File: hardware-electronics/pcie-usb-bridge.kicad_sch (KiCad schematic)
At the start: 62 parts, among them U10 24AA04T-I_OT, U3 PI7C9X440SLBFDE, Y1 ABM8-12.000MHZ-B2-T

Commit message: SCH cosmetic changes
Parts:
- added TP16, TP17: ~, symbol M2SmartHomeSymbols:TP_SMD_1mm
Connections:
- net at U3.21 (SMBCLK): now also TP16.
- net at U3.64 (SMBDATA): now also TP17.
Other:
- moved on the sheet: FB9, TP1, TP2, TP3, TP8

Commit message: SCH fill info box
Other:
- title: (none) -> M2SmartHome
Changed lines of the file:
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@@
 	(generator_version "8.0")
 	(paper "A4")
+	(title_block
+		(title "M2SmartHome")
+		(date "2024-10-11")
+		(rev "Rev 1.0.0")
+	)
 	(junction
 		(at 173.99 85.09)

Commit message: SCH update all symbols
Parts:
- C1, C2: footprint M2SmartHomeFootprints:CAPC1005X56N -> M2SmartHomeFootprints:C_0402
- R1, R3, R50, R51, R52, R53, R54: footprint R_5k1_0402:R_0402_1005Metric -> M2SmartHomeFootprints:R_0402
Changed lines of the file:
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@@
 			)
 		)
-		(property "Footprint" "R_5k1_0402:R_0402_1005Metric"
+		(property "Footprint" "M2SmartHomeFootprints:R_0402"
 			(at 111.76 101.6 0)
 			(effects
@@
 			)
 		)
-		(property "Footprint" "R_5k1_0402:R_0402_1005Metric"
+		(property "Footprint" "M2SmartHomeFootprints:R_0402"
 			(at 99.06 124.46 0)
 			(effects
@@
 			)
 		)
-		(property "Footprint" "R_5k1_0402:R_0402_1005Metric"
+		(property "Footprint" "M2SmartHomeFootprints:R_0402"
 			(at 102.87 101.6 0)
 			(effects
@@
 			)
 		)
-		(property "Footprint" "R_5k1_0402:R_0402_1005Metric"
+		(property "Footprint" "M2SmartHomeFootprints:R_0402"
 			(at 93.98 101.6 0)
 			(effects
@@
 			)
 		)
-		(property "Footprint" "R_5k1_0402:R_0402_1005Metric"
+		(property "Footprint" "M2SmartHomeFootprints:R_0402"
 			(at 90.17 81.28 0)
 			(effects
@@
 			)
 		)
-		(property "Footprint" "M2SmartHomeFootprints:CAPC1005X56N"
+		(property "Footprint" "M2SmartHomeFootprints:C_0402"
 			(at 177.8 148.59 0)
 			(effects
@@
 			)
 		)
-		(property "Footprint" "R_5k1_0402:R_0402_1005Metric"
+		(property "Footprint" "M2SmartHomeFootprints:R_0402"
 			(at 101.6 81.28 0)
 			(effects
@@
 			)
 		)
-		(property "Footprint" "M2SmartHomeFootprints:CAPC1005X56N"
+		(property "Footprint" "M2SmartHomeFootprints:C_0402"
 			(at 213.36 148.59 0)
 			(effects
@@
 			)
 		)
-		(property "Footprint" "R_5k1_0402:R_0402_1005Metric"
+		(property "Footprint" "M2SmartHomeFootprints:R_0402"
 			(at 110.49 124.46 0)
 			(effects

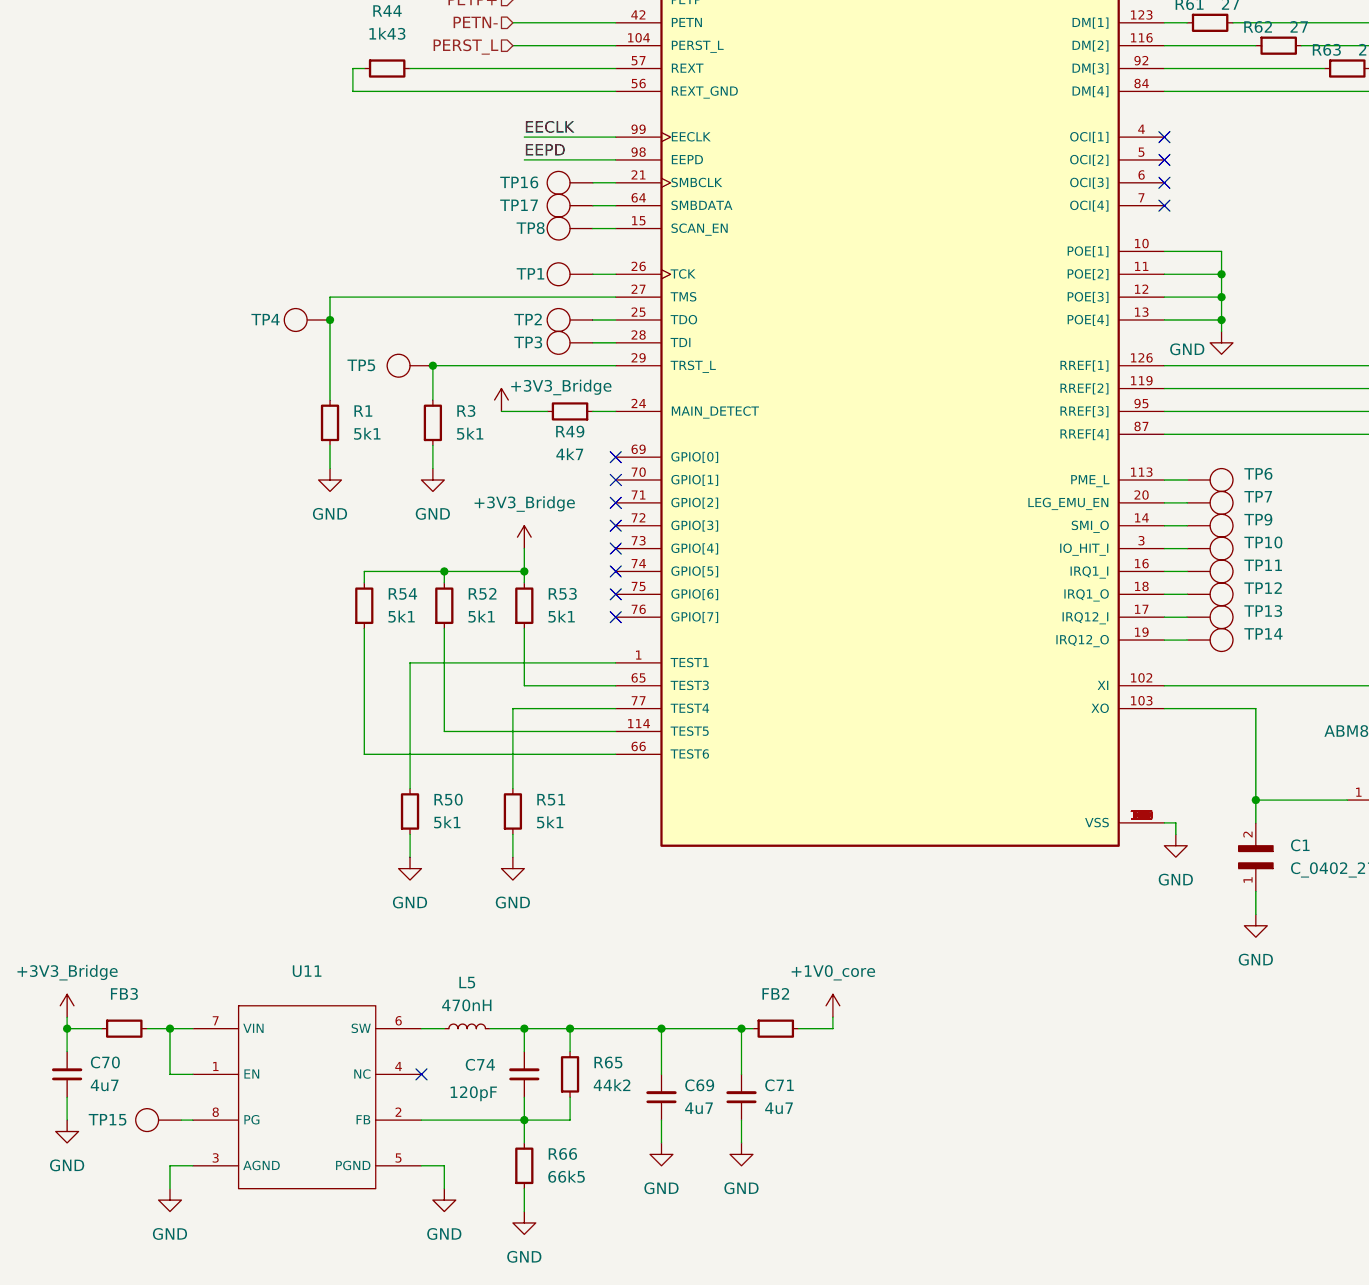
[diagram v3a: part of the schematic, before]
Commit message: [#13] BRD fix TP
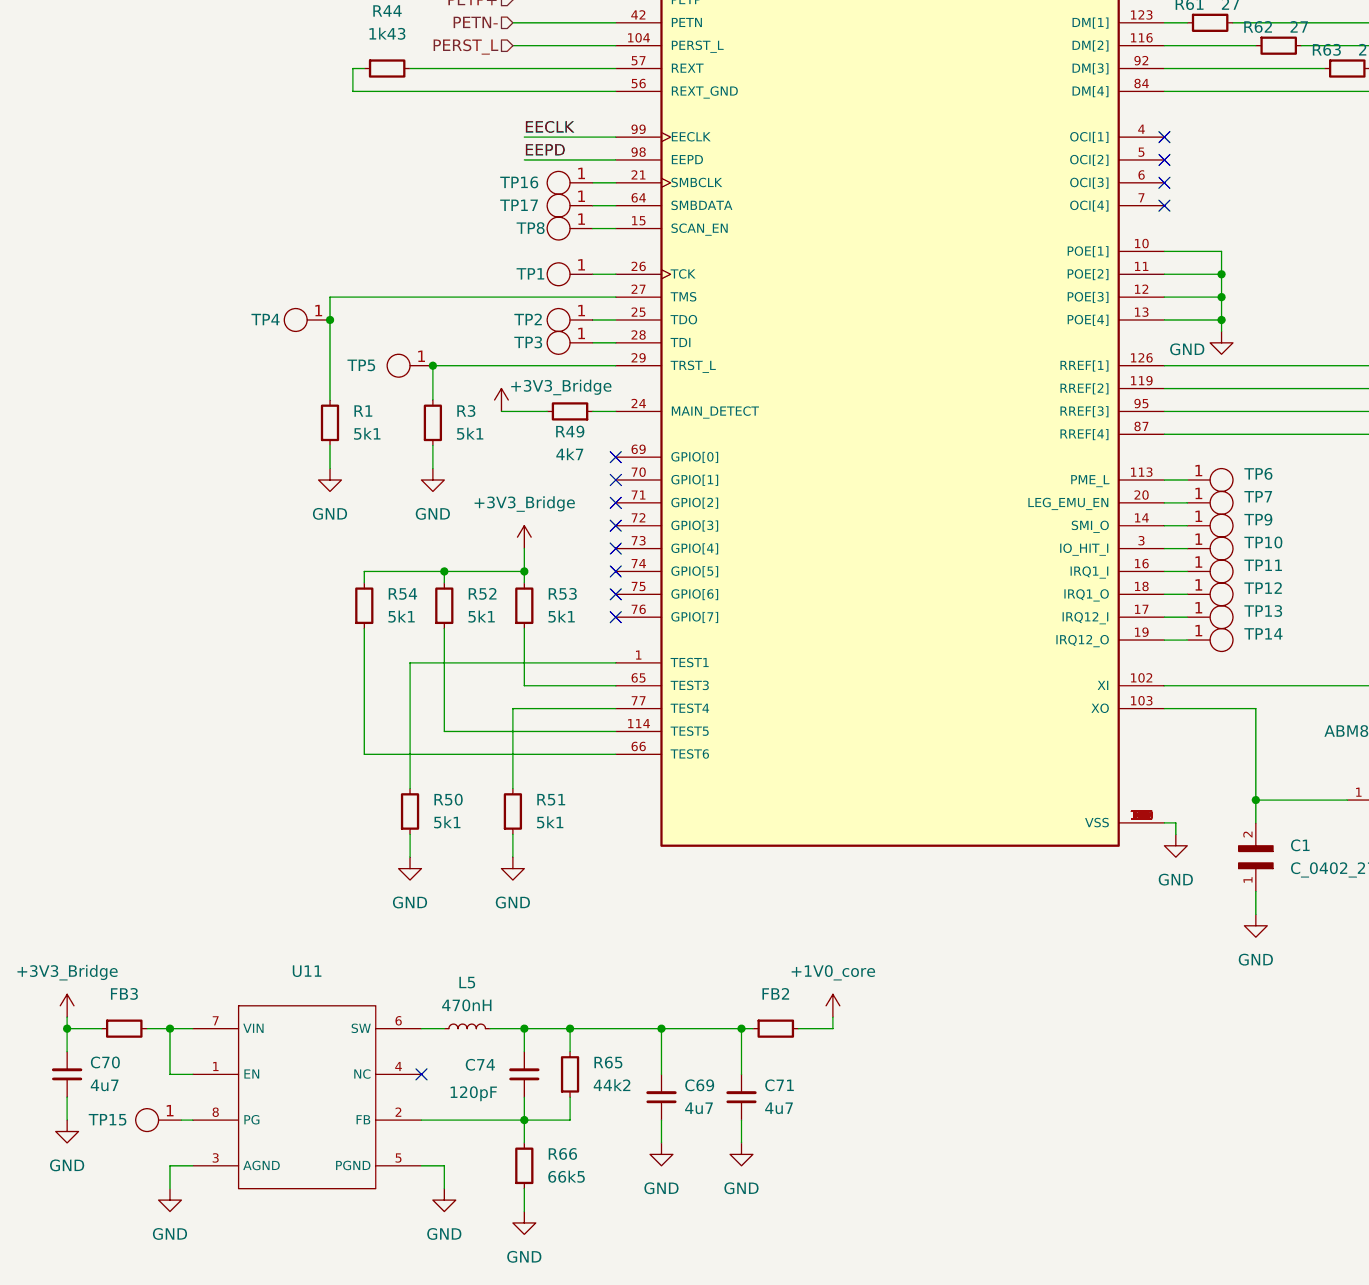
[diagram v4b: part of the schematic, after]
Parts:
- TP1, TP10, TP11, TP12, TP13, TP14, TP15, TP16, TP17, TP2, TP3, TP4, TP5, TP6, TP7, TP8, TP9: footprint (none) -> M2SmartHomeFootprints:TestPoint_Pad_D1.0mm
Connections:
- net at U3.21 (SMBCLK): now also TP16.1; no longer TP16.
- net at U11.8 (PG): now also TP15.1; no longer TP15.
- net at U3.20 (LEG_EMU_EN): now also TP7.1; no longer TP7.
- net at U3.25 (TDO): now also TP2.1; no longer TP2.
- net at U3.64 (SMBDATA): now also TP17.1; no longer TP17.
- net at U3.14 (SMI_O): now also TP9.1; no longer TP9.
- net at U3.15 (SCAN_EN): now also TP8.1; no longer TP8.
- net at U3.18 (IRQ1_O): now also TP12.1; no longer TP12.
- net at U3.17 (IRQ12_I): now also TP13.1; no longer TP13.
- net at U3.16 (IRQ1_I): now also TP11.1; no longer TP11.
- net at U3.3 (IO_HIT_I): now also TP10.1; no longer TP10.
- net at U3.19 (IRQ12_O): now also TP14.1; no longer TP14.
- net at R1.2, U3.27 (TMS): now also TP4.1; no longer TP4.
- net at U3.113 (PME_L): now also TP6.1; no longer TP6.
- net at R3.2, U3.29 (TRST_L): now also TP5.1; no longer TP5.
- net at U3.26 (TCK): now also TP1.1; no longer TP1.
- net at U3.28 (TDI): now also TP3.1; no longer TP3.
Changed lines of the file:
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@@
 			)
 		)
-		(property "Footprint" ""
+		(property "Footprint" "M2SmartHomeFootprints:TestPoint_Pad_D1.0mm"
 			(at 104.14 72.39 0)
 			(effects
@@
 			)
 		)
-		(pin ""
+		(pin "1"
 		)
 		(instances
@@
 			)
 		)
-		(property "Footprint" ""
+		(property "Footprint" "M2SmartHomeFootprints:TestPoint_Pad_D1.0mm"
 			(at 170.18 107.95 0)
 			(effects
@@
 			)
 		)
-		(pin ""
+		(pin "1"
 		)
 		(instances
@@
 			)
 		)
-		(property "Footprint" ""
+		(property "Footprint" "M2SmartHomeFootprints:TestPoint_Pad_D1.0mm"
 			(at 104.14 87.63 0)
 			(effects
@@
 			)
 		)
-		(pin ""
+		(pin "1"
 		)
 		(instances
@@
 			)
 		)
-		(property "Footprint" ""
+		(property "Footprint" "M2SmartHomeFootprints:TestPoint_Pad_D1.0mm"
 			(at 104.14 74.93 0)
 			(effects
@@
 			)
 		)
-		(pin ""
+		(pin "1"
 		)
 		(instances
@@
 			)
 		)
-		(property "Footprint" ""
+		(property "Footprint" "M2SmartHomeFootprints:TestPoint_Pad_D1.0mm"
 			(at 58.42 176.53 0)
 			(effects
@@
 			)
 		)
-		(pin ""
+		(pin "1"
 		)
 		(instances
@@
 			)
 		)
-		(property "Footprint" ""
+		(property "Footprint" "M2SmartHomeFootprints:TestPoint_Pad_D1.0mm"
 			(at 170.18 110.49 0)
 			(effects
@@
 			)
 		)
-		(pin ""
+		(pin "1"
 		)
 		(instances
@@
 			)
 		)
-		(property "Footprint" ""
+		(property "Footprint" "M2SmartHomeFootprints:TestPoint_Pad_D1.0mm"
 			(at 104.14 77.47 0)
 			(effects
@@
 			)
 		)
-		(pin ""
+		(pin "1"
 		)
 		(instances
@@
 			)
 		)
-		(property "Footprint" ""
+		(property "Footprint" "M2SmartHomeFootprints:TestPoint_Pad_D1.0mm"
 			(at 170.18 118.11 0)
 			(effects
@@
 			)
 		)
-		(pin ""
+		(pin "1"
 		)
 		(instances
@@
 			)
 		)
-		(property "Footprint" ""
+		(property "Footprint" "M2SmartHomeFootprints:TestPoint_Pad_D1.0mm"
 			(at 170.18 120.65 0)
 			(effects
@@
 			)
 		)
-		(pin ""
+		(pin "1"
 		)
 		(instances
@@
 			)
 		)
-		(property "Footprint" ""
+		(property "Footprint" "M2SmartHomeFootprints:TestPoint_Pad_D1.0mm"
 			(at 170.18 115.57 0)
 			(effects
@@
 			)
 		)
-		(pin ""
+		(pin "1"
 		)
 		(instances
@@
 			)
 		)
-		(property "Footprint" ""
+		(property "Footprint" "M2SmartHomeFootprints:TestPoint_Pad_D1.0mm"
 			(at 170.18 113.03 0)
 			(effects
@@
 			)
 		)
-		(pin ""
+		(pin "1"
 		)
 		(instances
@@
 			)
 		)
-		(property "Footprint" ""
+		(property "Footprint" "M2SmartHomeFootprints:TestPoint_Pad_D1.0mm"
 			(at 170.18 123.19 0)
 			(effects
@@
 			)
 		)
-		(pin ""
+		(pin "1"
 		)
 		(instances
@@
 			)
 		)
-		(property "Footprint" ""
+		(property "Footprint" "M2SmartHomeFootprints:TestPoint_Pad_D1.0mm"
 			(at 170.18 105.41 0)
 			(effects
@@
 			)
 		)
-		(pin ""
+		(pin "1"
 		)
 		(instances
@@
 			)
 		)
-		(property "Footprint" ""
+		(property "Footprint" "M2SmartHomeFootprints:TestPoint_Pad_D1.0mm"
 			(at 86.36 92.71 0)
 			(effects
@@
 			)
 		)
-		(pin ""
+		(pin "1"
 		)
 		(instances
@@
 			)
 		)
-		(property "Footprint" ""
+		(property "Footprint" "M2SmartHomeFootprints:TestPoint_Pad_D1.0mm"
 			(at 104.14 82.55 0)
 			(effects
@@
 			)
 		)
-		(pin ""
+		(pin "1"
 		)
 		(instances
@@
 			)
 		)
-		(property "Footprint" ""
+		(property "Footprint" "M2SmartHomeFootprints:TestPoint_Pad_D1.0mm"
 			(at 104.14 90.17 0)
 			(effects
@@
 			)
 		)
-		(pin ""
+		(pin "1"
 		)
 		(instances
@@
 			)
 		)
-		(property "Footprint" ""
+		(property "Footprint" "M2SmartHomeFootprints:TestPoint_Pad_D1.0mm"
 			(at 74.93 87.63 0)
 			(effects
@@
 			)
 		)
-		(pin ""
+		(pin "1"
 		)
 		(instances

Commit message: [#13] BRD fix 66k5 r and uSD slot
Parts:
- R66: footprint R_66k5_0402:R_0402_1005Metric -> M2SmartHomeFootprints:R_0402
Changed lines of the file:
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@@
 			)
 		)
-		(property "Footprint" "R_66k5_0402:R_0402_1005Metric"
+		(property "Footprint" "M2SmartHomeFootprints:R_0402"
 			(at 111.76 163.83 0)
 			(effects

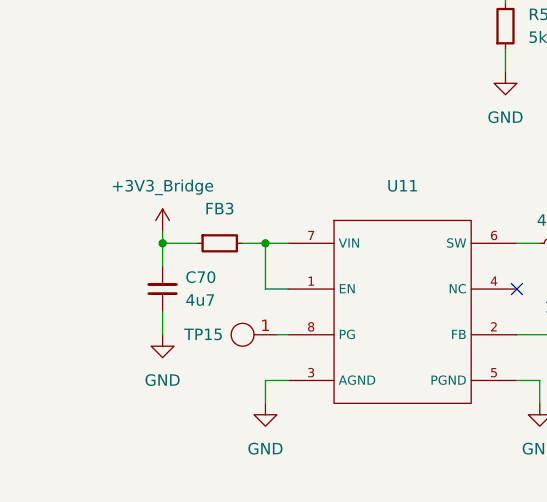
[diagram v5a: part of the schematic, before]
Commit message: [#13] WIP Placement PCIe bridge
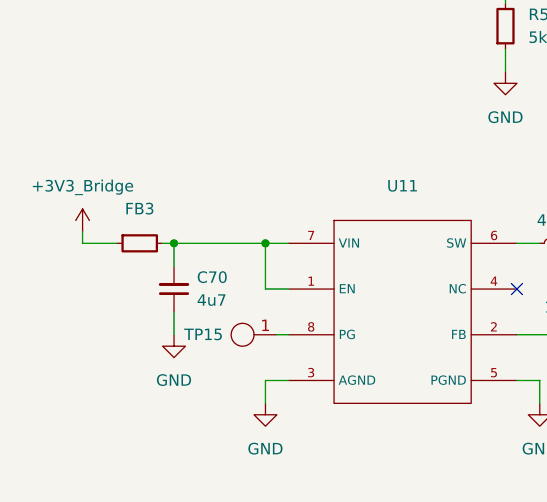
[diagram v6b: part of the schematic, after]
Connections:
- net +3V3_Bridge: no longer C70.2
- net at FB3.2, U11.1 (EN), U11.7 (VIN): now also C70.2
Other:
- moved on the sheet: C70, FB3
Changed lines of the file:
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@@
 	)
 	(junction
+		(at 46.99 166.37)
+		(diameter 0)
+		(color 0 0 0 0)
+	)
+	(junction
 		(at 96.52 166.37)
 		(diameter 0)
@@
 	)
 	(junction
-		(at 45.72 166.37)
-		(diameter 0)
-		(color 0 0 0 0)
-	)
-	(junction
 		(at 111.76 166.37)
 		(diameter 0)
@@
 	(wire
 		(pts
-			(xy 45.72 166.37) (xy 49.53 166.37)
+			(xy 36.83 166.37) (xy 40.64 166.37)
 		)
 		(stroke
@@
 	(wire
 		(pts
-			(xy 45.72 165.1) (xy 45.72 166.37)
+			(xy 36.83 165.1) (xy 36.83 166.37)
 		)
 		(stroke
@@
 	(wire
 		(pts
+			(xy 46.99 166.37) (xy 57.15 166.37)
+		)
+		(stroke
+			(width 0)
+			(type default)
+		)
+	)
+	(wire
+		(pts
 			(xy 74.93 85.09) (xy 106.68 85.09)
 		)
@@
 	(wire
 		(pts
-			(xy 45.72 166.37) (xy 45.72 168.91)
-		)
-		(stroke
-			(width 0)
-			(type default)
-		)
-	)
-	(wire
-		(pts
 			(xy 120.65 166.37) (xy 111.76 166.37)
 		)
@@
 	(wire
 		(pts
+			(xy 46.99 166.37) (xy 46.99 168.91)
+		)
+		(stroke
+			(width 0)
+			(type default)
+		)
+	)
+	(wire
+		(pts
 			(xy 87.63 181.61) (xy 87.63 184.15)
 		)
@@
 	(wire
 		(pts
-			(xy 54.61 166.37) (xy 57.15 166.37)
+			(xy 45.72 166.37) (xy 46.99 166.37)
 		)
 		(stroke
@@
 	(wire
 		(pts
-			(xy 45.72 173.99) (xy 45.72 176.53)
+			(xy 46.99 173.99) (xy 46.99 176.53)
 		)
 		(stroke
@@
 	(symbol
 		(lib_id "M2SmartHomeSymbols:FB_120R_0603")
-		(at 49.53 166.37 0)
+		(at 40.64 166.37 0)
 		(unit 1)
 		(exclude_from_sim no)
@@
 		(fields_autoplaced yes)
 		(property "Reference" "FB3"
-			(at 52.07 162.56 0)
+			(at 43.18 162.56 0)
 			(effects
 				(font
@@
 		)
 		(property "Value" "FB_120R_0603"
-			(at 69.85 176.53 0)
+			(at 60.96 176.53 0)
 			(effects
 				(font
@@
 		)
 		(property "Footprint" "M2SmartHomeFootprints:FB_0603"
-			(at 69.85 179.07 0)
+			(at 60.96 179.07 0)
 			(effects
 				(font
@@
 		)
 		(property "Datasheet" "https://www.murata.com/products/productdetail?partno=BLM18AG121SN1D"
-			(at 69.85 181.61 0)
+			(at 60.96 181.61 0)
 			(effects
 				(font
@@
 		)
 		(property "Description" "SMD Ferrite Bead, 120 Ω @ 100 MHz, 2 A, 0603 [1608 Metric], BLM18A Series"
-			(at 49.53 166.37 0)
+			(at 40.64 166.37 0)
 			(effects
 				(font
@@
 		)
 		(property "MPN" "BLM18AG121SN1D"
-			(at 69.85 184.15 0)
+			(at 60.96 184.15 0)
 			(effects
 				(font
@@
 		)
 		(property "Manufacturer" "Murata"
-			(at 69.85 186.69 0)
+			(at 60.96 186.69 0)
 			(effects
 				(font
@@
 		)
 		(property "License" "Apache-2.0"
-			(at 69.85 189.23 0)
+			(at 60.96 189.23 0)
 			(effects
 				(font
@@
 		)
 		(property "Author" "Your Name"
-			(at 69.85 191.77 0)
+			(at 60.96 191.77 0)
 			(effects
 				(font
@@
 		)
 		(property "Impedance" "120R @ 100 MHz"
-			(at 69.85 194.31 0)
+			(at 60.96 194.31 0)
 			(effects
 				(font
@@
 		)
 		(property "Current" "2A"
-			(at 69.85 196.85 0)
+			(at 60.96 196.85 0)
 			(effects
 				(font
@@
 	(symbol
 		(lib_id "power:+3V3")
-		(at 45.72 165.1 0)
+		(at 36.83 165.1 0)
 		(unit 1)
 		(exclude_from_sim no)
@@
 		(fields_autoplaced yes)
 		(property "Reference" "#PWR0196"
-			(at 45.72 168.91 0)
+			(at 36.83 168.91 0)
 			(effects
 				(font
@@
 		)
 		(property "Value" "+3V3_Bridge"
-			(at 45.72 160.02 0)
+			(at 36.83 160.02 0)
 			(effects
 				(font
@@
 		)
 		(property "Footprint" ""
-			(at 45.72 165.1 0)
+			(at 36.83 165.1 0)
 			(effects
 				(font
@@
 		)
 		(property "Datasheet" ""
-			(at 45.72 165.1 0)
+			(at 36.83 165.1 0)
 			(effects
 				(font
@@
 		)
 		(property "Description" "Power symbol creates a global label with name \"+3V3\""
-			(at 45.72 165.1 0)
+			(at 36.83 165.1 0)
 			(effects
 				(font
@@
 	(symbol
 		(lib_id "power:GND")
-		(at 45.72 176.53 0)
+		(at 46.99 176.53 0)
 		(unit 1)
 		(exclude_from_sim no)
@@
 		(fields_autoplaced yes)
 		(property "Reference" "#PWR0197"
-			(at 45.72 182.88 0)
+			(at 46.99 182.88 0)
 			(effects
 				(font
@@
 		)
 		(property "Value" "GND"
-			(at 45.72 181.61 0)
+			(at 46.99 181.61 0)
 			(effects
 				(font
@@
 		)
 		(property "Footprint" ""
-			(at 45.72 176.53 0)
+			(at 46.99 176.53 0)
 			(effects
 				(font
@@
 		)
 		(property "Datasheet" ""
-			(at 45.72 176.53 0)
+			(at 46.99 176.53 0)
 			(effects
 				(font
@@
 		)
 		(property "Description" "Power symbol creates a global label with name \"GND\" , ground"
-			(at 45.72 176.53 0)
+			(at 46.99 176.53 0)
 			(effects
 				(font
@@
 	(symbol
 		(lib_id "M2SmartHomeSymbols:C_4u7_0402")
-		(at 45.72 173.99 90)
+		(at 46.99 173.99 90)
 		(unit 1)
 		(exclude_from_sim no)
@@
 		(fields_autoplaced yes)
 		(property "Reference" "C70"
-			(at 48.26 170.1736 90)
+			(at 49.53 170.1736 90)
 			(effects
 				(font
@@
 		)
 		(property "Value" "C_4u7_0402"
-			(at 55.88 153.67 0)
+			(at 57.15 153.67 0)
 			(effects
 				(font
@@
 		)
 		(property "Footprint" "M2SmartHomeFootprints:C_0402"
-			(at 58.42 153.67 0)
+			(at 59.69 153.67 0)
 			(effects
 				(font
@@
 		)
 		(property "Datasheet" "https://www.murata.com/products/productdetail?partno=GRM155R60J475ME47%23"
-			(at 60.96 153.67 0)
+			(at 62.23 153.67 0)
 			(effects
 				(font
@@
 		)
 		(property "Description" "SMD Multilayer Ceramic Capacitor, 4.7 µF, 6.3 V, 0402 [1005 Metric], ±20%, X5R, GRM Series"
-			(at 45.72 173.99 0)
+			(at 46.99 173.99 0)
 			(effects
 				(font
@@
 		)
 		(property "MPN" "GRM155R60J475ME47D"
-			(at 63.5 153.67 0)
+			(at 64.77 153.67 0)
 			(effects
 				(font
@@
 		)
 		(property "Manufacturer" "Murata"
-			(at 66.04 153.67 0)
+			(at 67.31 153.67 0)
 			(effects
 				(font
@@
 		)
 		(property "License" "Apache-2.0"
-			(at 68.58 153.67 0)
+			(at 69.85 153.67 0)
 			(effects
 				(font
@@
 		)
 		(property "Author" "Your Name"
-			(at 71.12 153.67 0)
+			(at 72.39 153.67 0)
 			(effects
 				(font
@@
 		)
 		(property "Val" "4u7"
-			(at 48.26 172.7136 90)
+			(at 49.53 172.7136 90)
 			(effects
 				(font
@@
 		)
 		(property "Voltage" "6.3V"
-			(at 73.66 153.67 0)
+			(at 74.93 153.67 0)
 			(effects
 				(font
@@
 		)
 		(property "Dielectric" "X5R"
-			(at 76.2 153.67 0)
+			(at 77.47 153.67 0)
 			(effects
 				(font
